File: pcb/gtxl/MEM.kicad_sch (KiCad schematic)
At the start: 4 parts, among them U13 HM62256BLP, U14 27C256, U15 74AHCT04, U16 74LS21

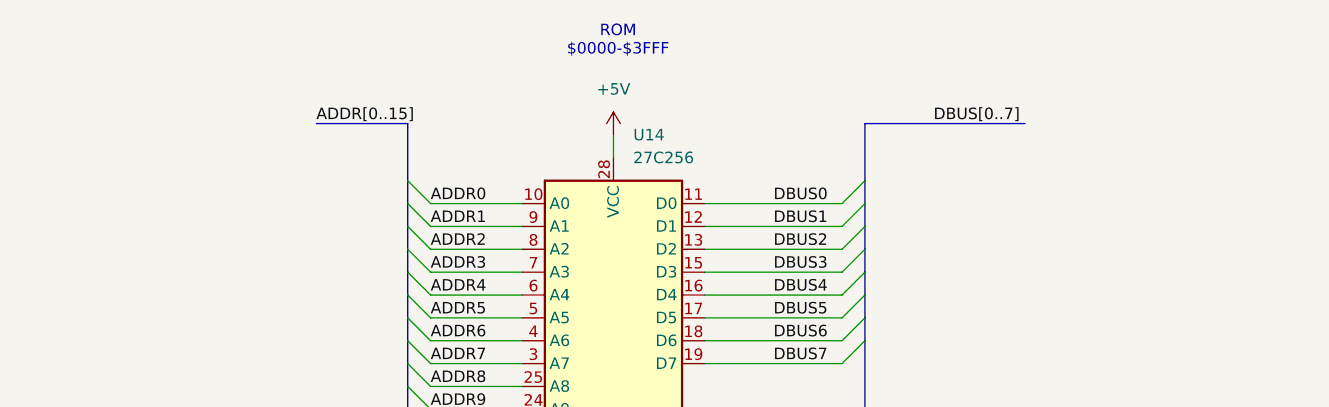
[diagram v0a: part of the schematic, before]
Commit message: Update schematic with removed timer.  Update video timing notes.
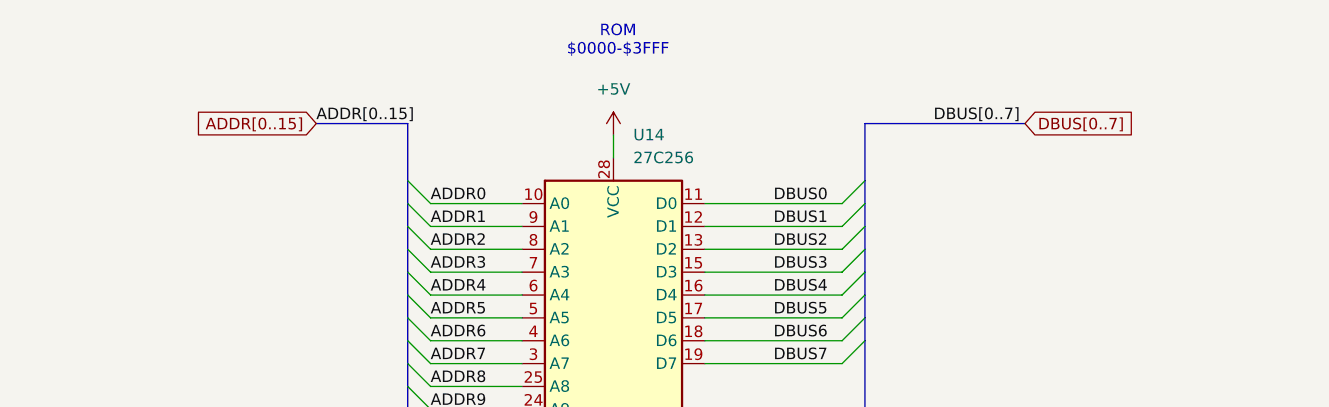
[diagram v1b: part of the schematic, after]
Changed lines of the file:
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@@
+		)
+	)
+	(global_label "ADDR[0..15]"
+		(shape input)
+		(at 175.26 52.07 180)
+		(fields_autoplaced yes)
+		(effects
+			(font
+				(size 1.27 1.27)
+			)
+			(justify right)
+		)
+		(property "Intersheetrefs" "${INTERSHEET_REFS}"
+			(at 160.8447 52.07 0)
+			(effects
+				(font
+					(size 1.27 1.27)
+				)
+				(justify right)
+				(hide yes)
+			)
 		)
 	)
@@
 				(hide yes)
 			)
+		)
+	)
+	(global_label "DBUS[0..7]"
+		(shape input)
+		(at 254 52.07 0)
+		(fields_autoplaced yes)
+		(effects
+			(font
+				(size 1.27 1.27)
+			)
+			(justify left)
+		)
+		(property "Intersheetrefs" "${INTERSHEET_REFS}"
+			(at 267.3872 52.07 0)
+			(effects
+				(font
+					(size 1.27 1.27)
+				)
+				(justify left)
+				(hide yes)
+			)
